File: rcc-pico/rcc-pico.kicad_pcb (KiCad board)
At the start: 2 copper layers, 71.2 x 56 mm, 52 parts, among them J1 Conn_02x02_Odd_Even, J10 Conn_02x04_Odd_Even, J11 Conn_02x04_Odd_Even, J12 Conn_02x04_Odd_Even, J14 Conn_02x05_Odd_Even, J16 Conn_01x02_Pin, J3 PJ-006A, J5 Conn_3x4_female, J7 Conn_03x10, J8 Screw_Terminal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

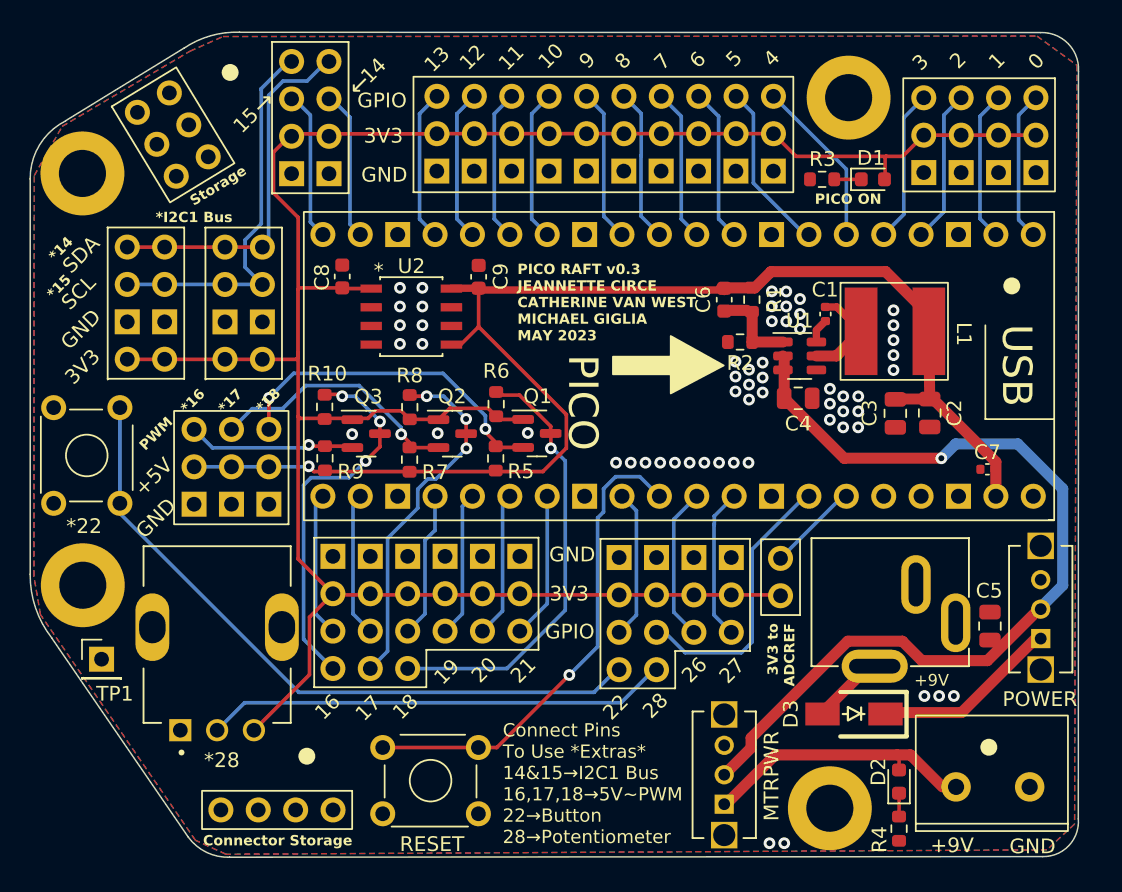
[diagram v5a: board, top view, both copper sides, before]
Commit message: v0.3 for ordering, cleaned up screenprint and rearranged 9v cap to be next to the diode for ease
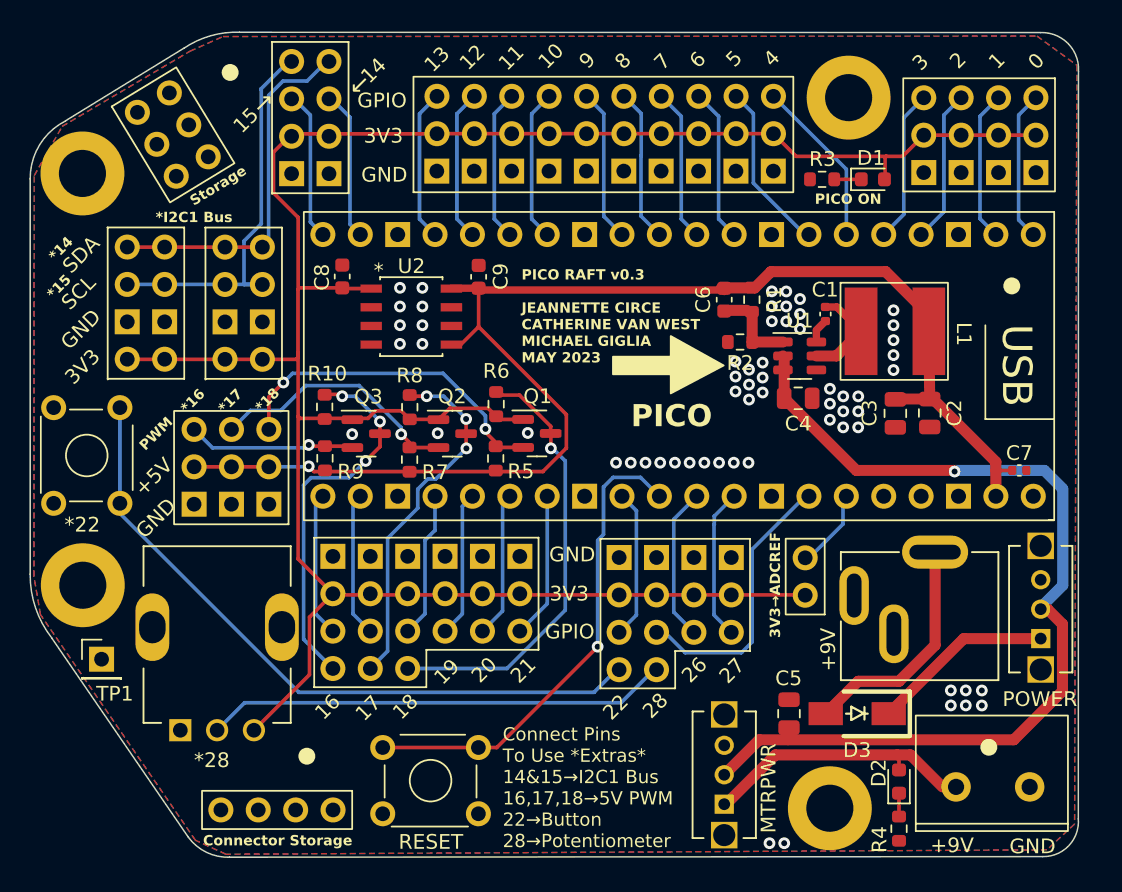
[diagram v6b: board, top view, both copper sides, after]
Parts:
- moved C5 14.9 mm to (127.8, 74.7)
- moved J3 8.77 mm to (137.7, 63.7), turned to 0 degrees
- moved C7 2.17 mm to (143.4, 58.1), turned to 180 degrees
- moved J16 1.68 mm to (128.9, 64.1)
- moved D3 0.23 mm to (132.4, 74.7)
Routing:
- net Net-(D3-A): track 4.86 -> 15.7 mm
- net +9V: track 61.5 -> 65.8 mm
- net +3.3V: track 162.1 -> 163.3 mm
- net +5V: track 91.3 -> 92.4 mm
- net /SCL: track 26.3 -> 27.1 mm
- net /adcref_3v3: track 5.93 -> 5.14 mm
- net GND: vias 58 -> 61
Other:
- board text added: "3V3→ADCREF"
- board text added: "Connect Pins To Use *Extras* 14&15→I2C1 Bus 16,17,18→5V PWM 22→Button 28→Potentiometer"
- board text removed: "3V3 to ADCREF"
- board text removed: "Connect Pins To Use *Extras* 14&15→I2C1 Bus 16,17,18→5V~PWM 22→Button 28→Potentiometer"
